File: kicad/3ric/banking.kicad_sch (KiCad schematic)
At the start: 33 parts

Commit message: updates to logisim project and schematics
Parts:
- removed U? (x4): (no value), symbol 74xx:74LS08
- removed U? (x7): (no value), symbol 74xx:74LS32
- removed U? (x2): 74LS08, symbol 74xx:74LS08
- removed U?: (no value), symbol 74xx:74LS00
- removed U? (x2): 74LS32, symbol 74xx:74LS32
- added U? (x9): 74LS32, symbol 74xx:74LS32
- added U? (x5): 74LS08, symbol 74xx:74LS08
- added U?: 74LS00, symbol 74xx:74LS00
- U? (x4): value (none) -> 74LS112
- U?: value (none) -> 74LS32
- U? (x3): value (none) -> 74LS00
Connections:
- net B1: now also U?.6, U?.9
- net B2: now also U?.5, U?.8
- net BSS: now also U?.10, U?.13, U?.2, U?.5
- net PHI2: now also U?.9
- net VCC: now also U?.4 (~{S})
- net X0: now also U?.10
- net X1: now also U?.4
- net X2: now also U?.1
- net X3: now also U?.13
- net X8: now also U?.9
- net X9: now also U?.5
- net XA: now also U?.2
- net XB: now also U?.12
- net at U?.10, U?.4: now also U?.6
- net at U?.5: now also U?.13, U?.3
- net at U?.3 (J): now also U?.11
- net at U?.1, U?.12: now also U?.8; no longer U?.6
- net at U?.12: now also U?.1 (C)
- net at U?.13: now also U?.11
- net at U?.1, U?.9: now also U?.11
- net at U?.2: now also U?.12, U?.8
- net BANK renamed RAMREAD
- net READROM renamed ROMREAD
- new net: U?.12, U?.3
- new net: U?.1, U?.11
- new net: U?.10, U?.6
- new net: U?.6, U?.9
- new net: U?.4, U?.8
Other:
- moved on the sheet: U?A, U?B, U?C, U?D, U?F

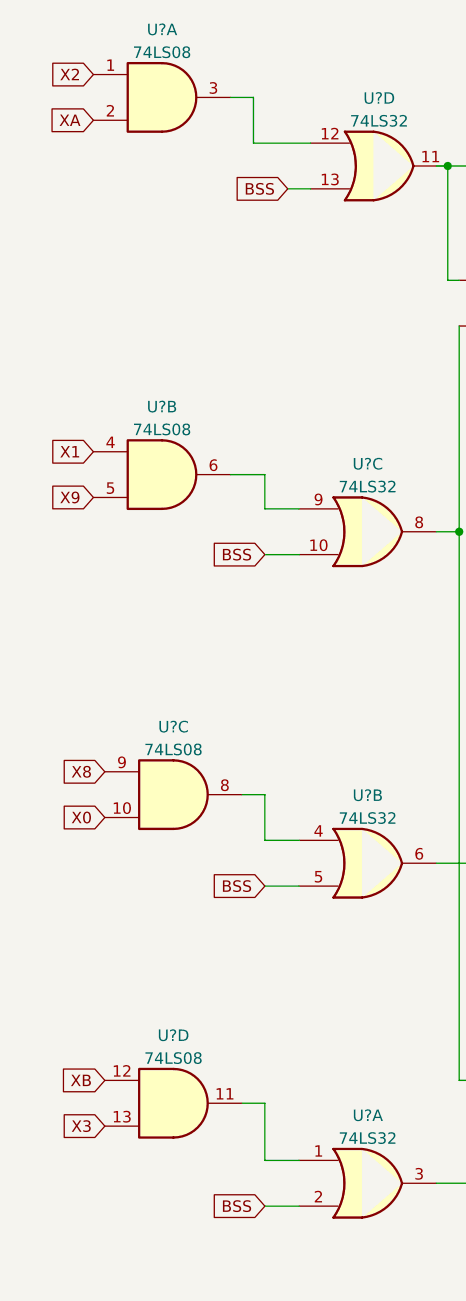
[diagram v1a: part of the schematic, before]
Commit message: move some of the logic to PLD, move device range from C1XX to CX00 update device labels to be more correct update PLD
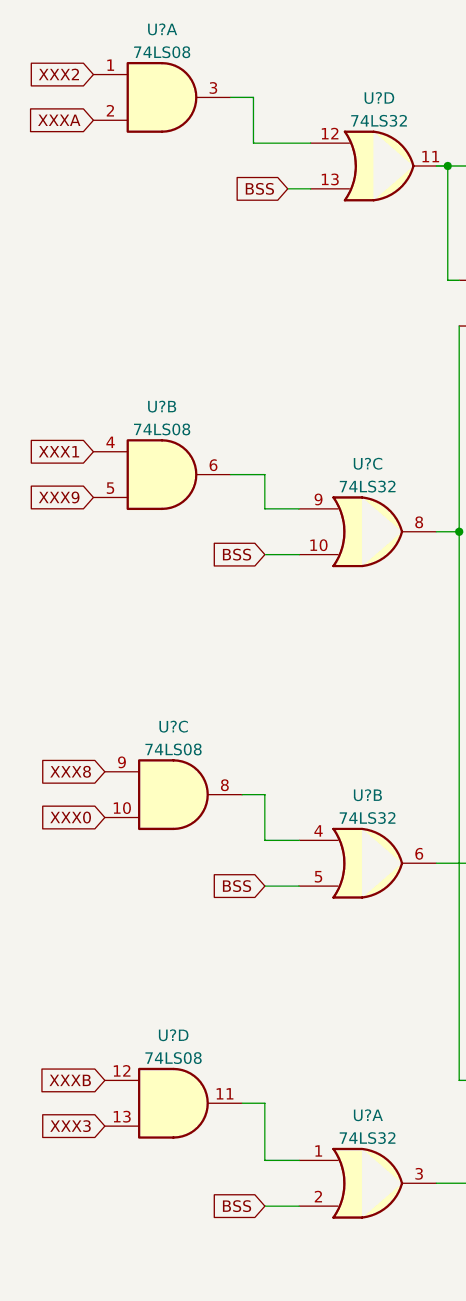
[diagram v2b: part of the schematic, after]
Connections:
- net X0 renamed XXX0
- net X1 renamed XXX1
- net X2 renamed XXX2
- net X3 renamed XXX3
- net X8 renamed XXX8
- net X9 renamed XXX9
- net XA renamed XXXA
- net XB renamed XXXB
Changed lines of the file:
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@@
     )
   )
-  (global_label "X8" (shape input) (at 33.02 99.06 180) (fields_autoplaced)
+  (global_label "XXX8" (shape input) (at 33.02 99.06 180) (fields_autoplaced)
     (effects (font (size 1.27 1.27)) (justify right))
-    (property "Intersheet References" "${INTERSHEET_REFS}" (id 0) (at 28.1879 98.9806 0)
+    (property "Intersheet References" "${INTERSHEET_REFS}" (id 0) (at 25.7688 98.9806 0)
       (effects (font (size 1.27 1.27)) (justify right) hide)
     )
@@
     )
   )
-  (global_label "XA" (shape input) (at 31.75 26.67 180) (fields_autoplaced)
+  (global_label "XXXA" (shape input) (at 31.75 26.67 180) (fields_autoplaced)
     (effects (font (size 1.27 1.27)) (justify right))
-    (property "Intersheet References" "${INTERSHEET_REFS}" (id 0) (at 27.0388 26.5906 0)
+    (property "Intersheet References" "${INTERSHEET_REFS}" (id 0) (at 24.6198 26.5906 0)
       (effects (font (size 1.27 1.27)) (justify right) hide)
     )
   )
-  (global_label "X3" (shape input) (at 33.02 138.43 180) (fields_autoplaced)
+  (global_label "XXX3" (shape input) (at 33.02 138.43 180) (fields_autoplaced)
     (effects (font (size 1.27 1.27)) (justify right))
-    (property "Intersheet References" "${INTERSHEET_REFS}" (id 0) (at 28.1879 138.3506 0)
+    (property "Intersheet References" "${INTERSHEET_REFS}" (id 0) (at 25.7688 138.3506 0)
       (effects (font (size 1.27 1.27)) (justify right) hide)
     )
@@
     )
   )
-  (global_label "X0" (shape input) (at 33.02 104.14 180) (fields_autoplaced)
+  (global_label "XXX0" (shape input) (at 33.02 104.14 180) (fields_autoplaced)
     (effects (font (size 1.27 1.27)) (justify right))
-    (property "Intersheet References" "${INTERSHEET_REFS}" (id 0) (at 28.1879 104.0606 0)
+    (property "Intersheet References" "${INTERSHEET_REFS}" (id 0) (at 25.7688 104.0606 0)
       (effects (font (size 1.27 1.27)) (justify right) hide)
     )
   )
-  (global_label "XB" (shape input) (at 33.02 133.35 180) (fields_autoplaced)
+  (global_label "XXXB" (shape input) (at 33.02 133.35 180) (fields_autoplaced)
     (effects (font (size 1.27 1.27)) (justify right))
-    (property "Intersheet References" "${INTERSHEET_REFS}" (id 0) (at 28.1274 133.2706 0)
+    (property "Intersheet References" "${INTERSHEET_REFS}" (id 0) (at 25.7083 133.2706 0)
       (effects (font (size 1.27 1.27)) (justify right) hide)
     )
@@
     )
   )
-  (global_label "X2" (shape input) (at 31.75 21.59 180) (fields_autoplaced)
+  (global_label "XXX2" (shape input) (at 31.75 21.59 180) (fields_autoplaced)
     (effects (font (size 1.27 1.27)) (justify right))
-    (property "Intersheet References" "${INTERSHEET_REFS}" (id 0) (at 26.9179 21.5106 0)
+    (property "Intersheet References" "${INTERSHEET_REFS}" (id 0) (at 24.4988 21.5106 0)
       (effects (font (size 1.27 1.27)) (justify right) hide)
     )
@@
     )
   )
-  (global_label "X9" (shape input) (at 31.75 68.58 180) (fields_autoplaced)
+  (global_label "XXX9" (shape input) (at 31.75 68.58 180) (fields_autoplaced)
     (effects (font (size 1.27 1.27)) (justify right))
-    (property "Intersheet References" "${INTERSHEET_REFS}" (id 0) (at 26.9179 68.5006 0)
+    (property "Intersheet References" "${INTERSHEET_REFS}" (id 0) (at 24.4988 68.5006 0)
       (effects (font (size 1.27 1.27)) (justify right) hide)
     )
   )
-  (global_label "X1" (shape input) (at 31.75 63.5 180) (fields_autoplaced)
+  (global_label "XXX1" (shape input) (at 31.75 63.5 180) (fields_autoplaced)
     (effects (font (size 1.27 1.27)) (justify right))
-    (property "Intersheet References" "${INTERSHEET_REFS}" (id 0) (at 26.9179 63.4206 0)
+    (property "Intersheet References" "${INTERSHEET_REFS}" (id 0) (at 24.4988 63.4206 0)
       (effects (font (size 1.27 1.27)) (justify right) hide)
     )

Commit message: push schematic updates
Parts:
- removed U? (x6): 74LS32, symbol 74xx:74LS32
- added LS?: Speaker, symbol Device:Speaker
- added U? (x4): 74LS08, symbol 74xx:74LS08
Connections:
- net GND: now also LS?.2
- net VCC: now also U?.10 (~{S}), U?.11 (J), U?.12 (K), U?.14 (~{R}); no longer U?.10 (~{S})
- net XXX0: now also U?.9; no longer U?.10
- net XXX3: now also U?.12; no longer U?.13
- net XXX8: now also U?.10; no longer U?.9
- net XXXB: now also U?.13; no longer U?.12
- net C030: now reaches U?.13 (C)
- net at U?.9 (Q): now also LS?.1
- new net ~{RESET}: U?.10 (~{S})

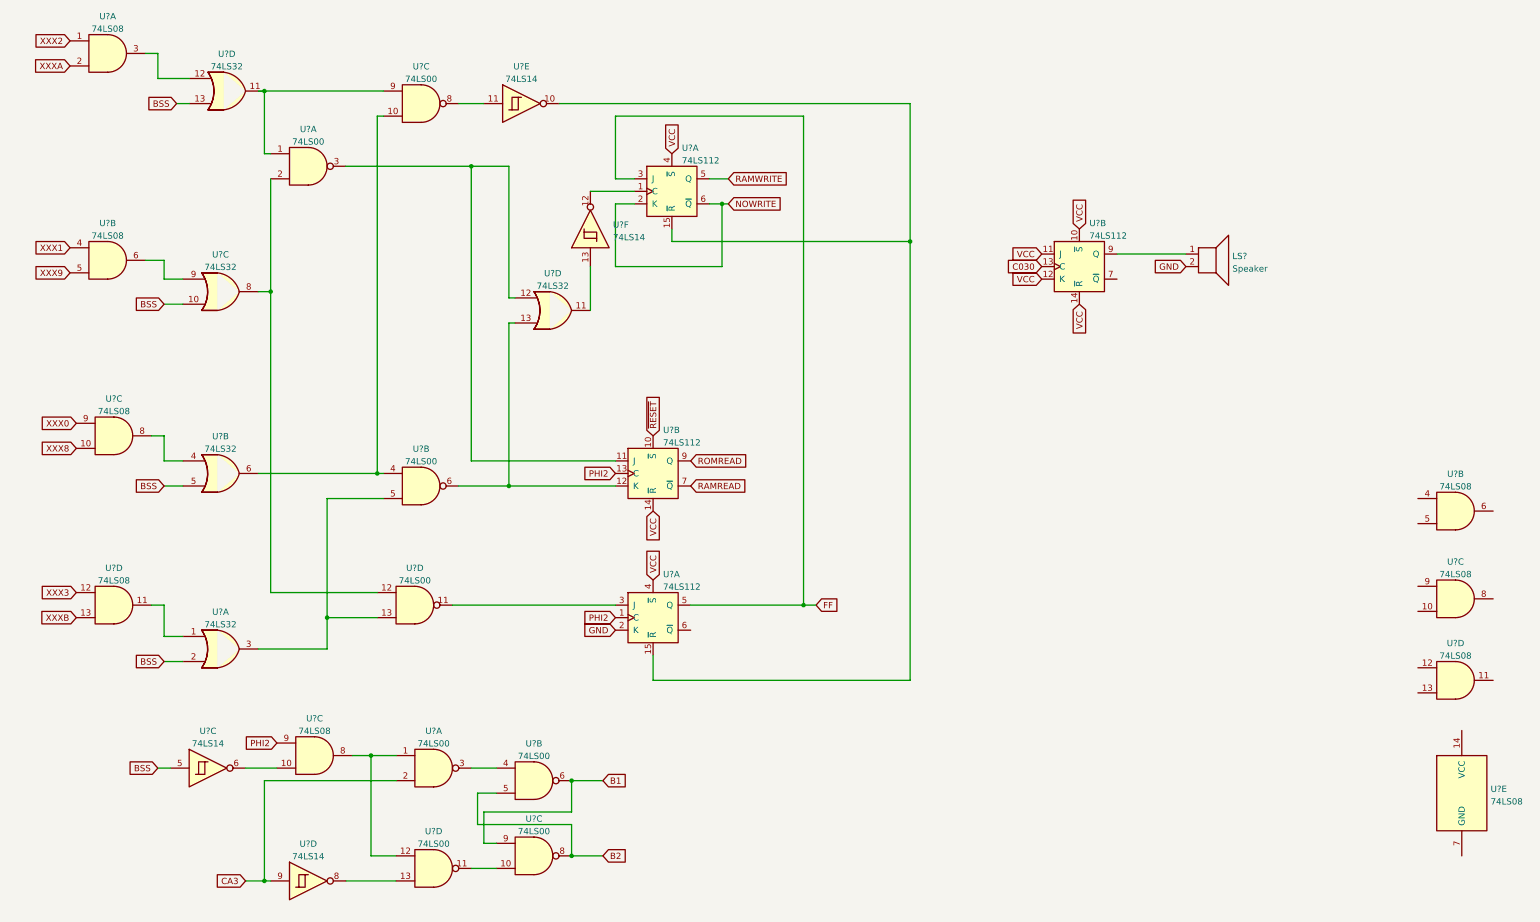
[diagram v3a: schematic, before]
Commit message: upgraded to kicad 8, updates to schematic - added snes controllers, mouse port, many fixes
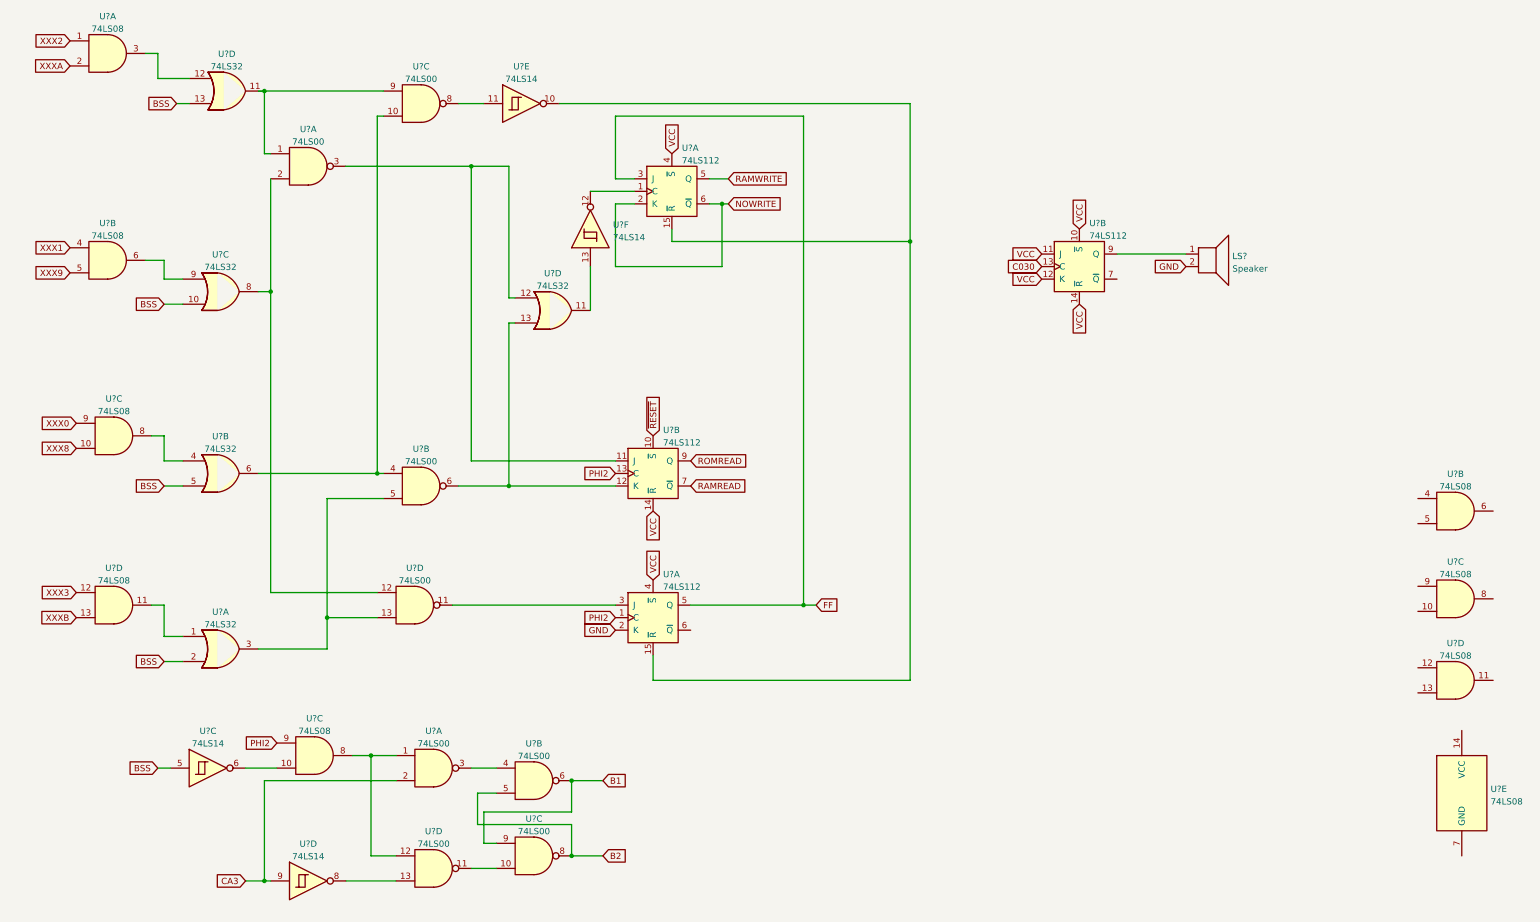
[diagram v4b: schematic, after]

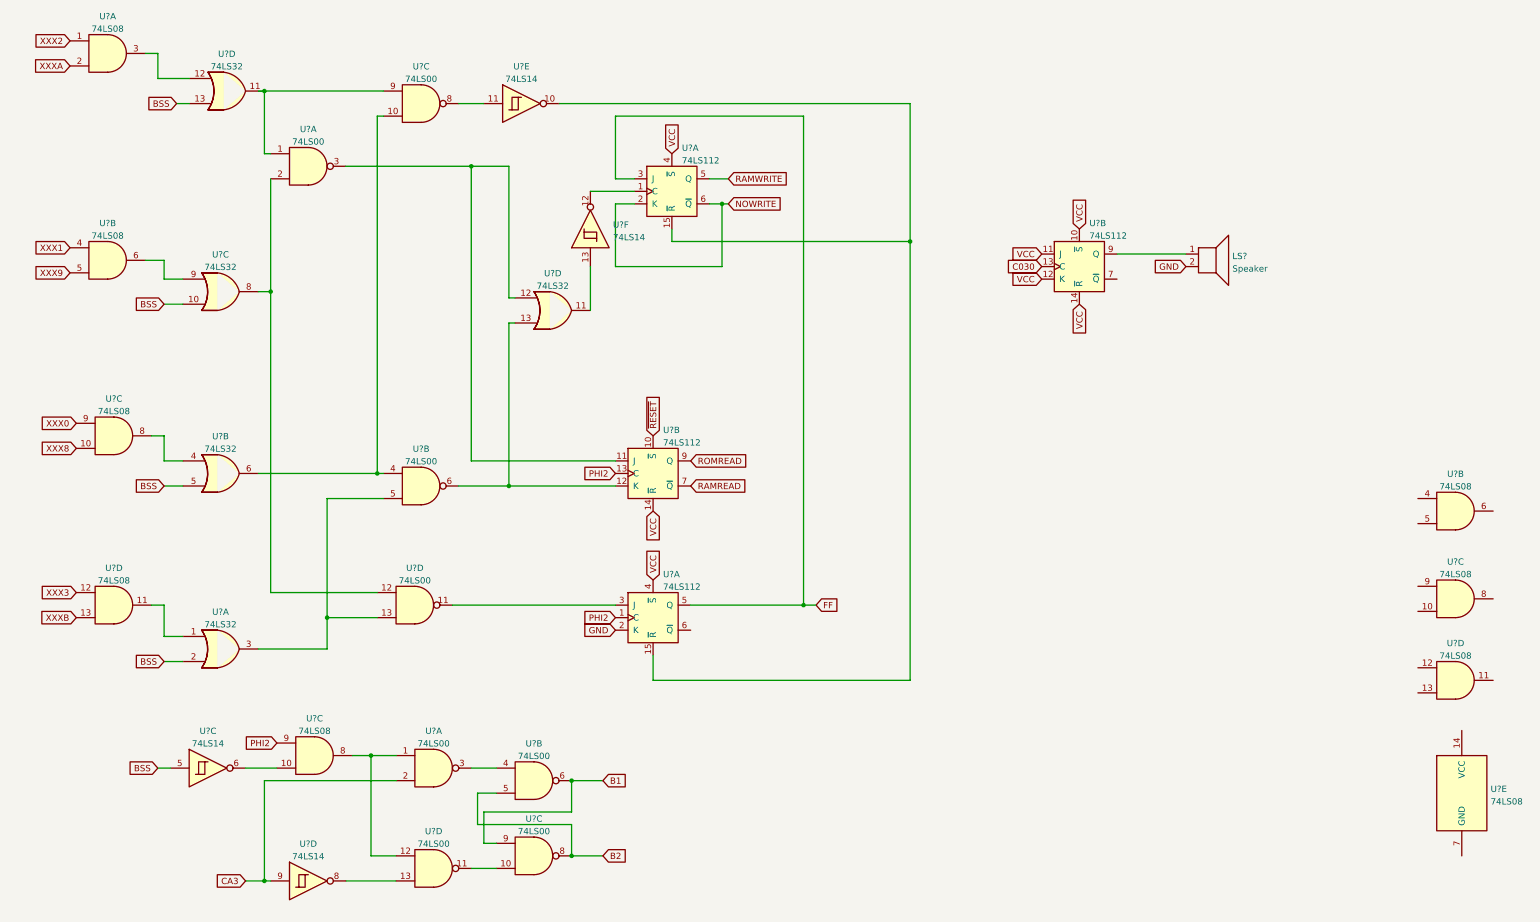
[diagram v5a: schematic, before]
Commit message: update schematic based on breadboard
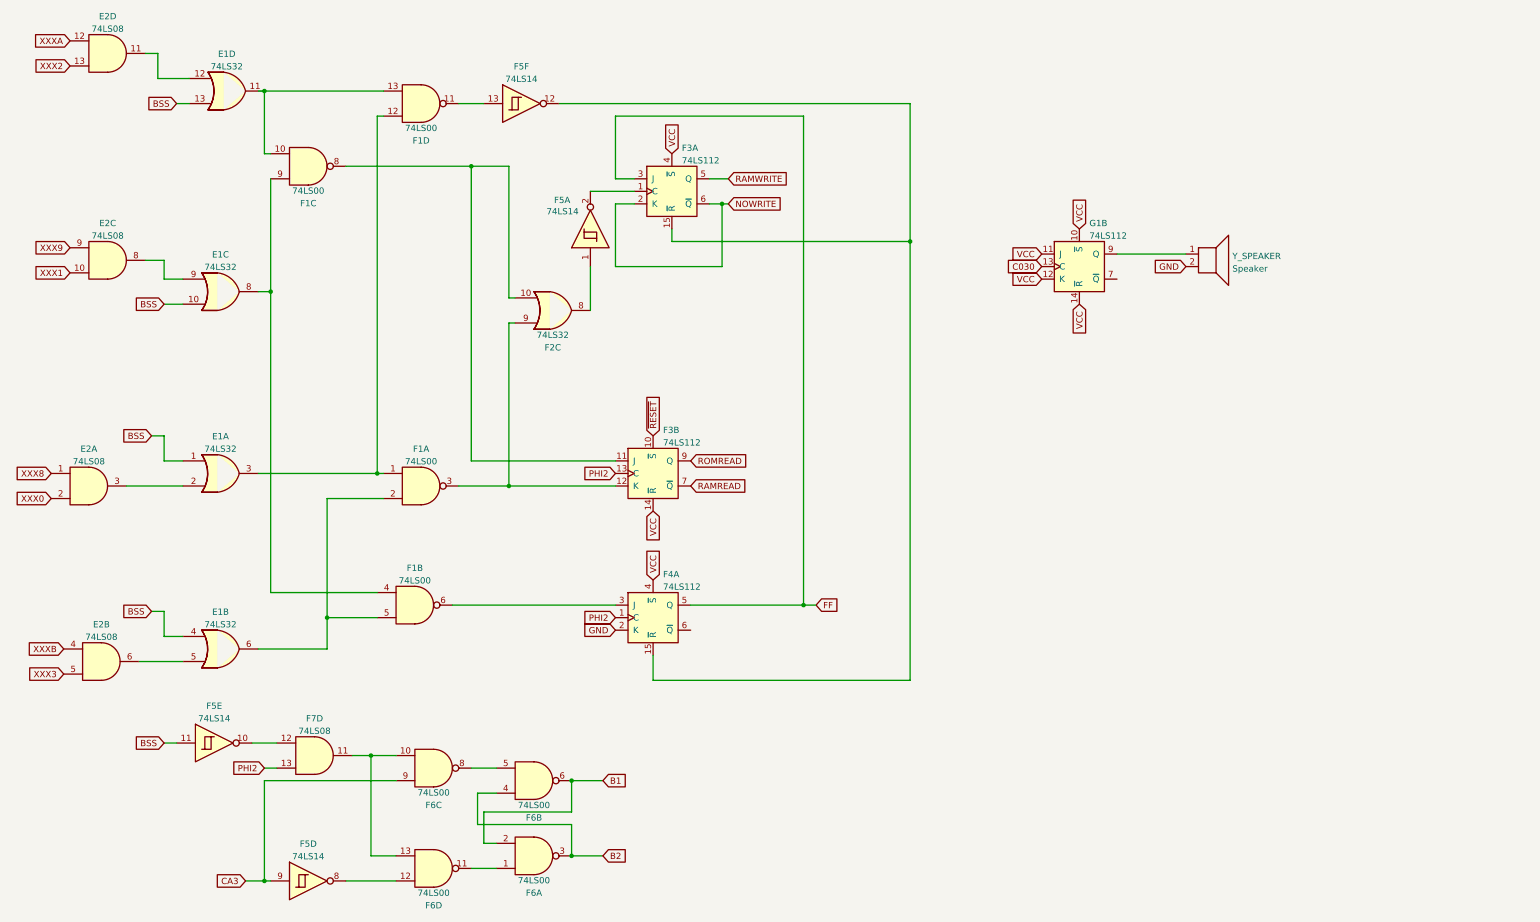
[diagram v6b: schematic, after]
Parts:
- removed U? (x6): 74LS08, symbol 74xx:74LS08
- removed U?: 74LS14, symbol 74xx:74LS14
- added unit 1 of E2
- added unit 2 of E2
- added unit 5 of F5
- gave numbers to parts that had none: 11
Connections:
- net B1: now also F6.2; no longer F6.9
- net B2: now also F6.3, F6.4; no longer F6.5, F6.8
- net BSS: now also E1.1, E1.4, F5.11; no longer E1.2, E1.5
- net CA3: now also F6.9; no longer F6.2
- net PHI2: now also F7.13; no longer F7.9
- net XXX0: now also E2.2
- net XXX1: now also E2.10; no longer E2.4
- net XXX2: now also E2.13; no longer E2.1
- net XXX3: now also E2.5
- net XXX8: now also E2.1
- net XXX9: now also E2.9; no longer E2.5
- net XXXA: now also E2.12; no longer E2.2
- net XXXB: now also E2.4
- net at E1.12: now also E2.11; no longer E2.3
- net at F3.15 (~{R}), F4.15 (~{R}): now also F5.12; no longer F5.10
- net at F4.3 (J): now also F1.6; no longer F1.11
- net at F6.11: now also F6.1; no longer F6.10
- net at E1.9: now also E2.8; no longer E2.6
- net at F3.1 (C): now also F5.2; no longer F5.12
- net at F6.13: now also F6.10, F7.11; no longer F5.8
- new net: E1.11, F1.10, F1.13
- new net: F1.11, F5.13
- new net: F5.10, F7.12
- new net: E1.8, F1.4, F1.9
- new net: E1.6, F1.2, F1.5
- new net: E1.2, E2.3
- new net: E1.3, F1.1, F1.12
- new net: E1.5, E2.6
- new net: F2.8, F5.1
- new net: F1.8, F2.10, F3.11 (J)
- new net: F1.3, F2.9, F3.12 (K)
- new net: F5.8, F6.12
- new net: F6.5, F6.8
